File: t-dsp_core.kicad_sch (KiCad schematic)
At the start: 209 parts, among them IC1 Logic Level Shifter - 74HCT2G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, J1 jumper, J10 JST-XH Connector, J11 JST-XH Connector, J12 RGB LED HEADEER, J13 Conn_01x02, J14 Conn_01x03, J15 Conn_01x01, J16 Conn_01x02, J17 Conn_02x04_Odd_Even, J18 Conn_02x02_Odd_Even, J19 Conn_01x01, J2 GROUND HEADER, J20 Conn_01x01, J21 jumper, J22 35RAPC4BV4, J23 35RAPC4BV4, J24 Conn_01x04, J25 PRT-14417, J26 73725-0110BLF, J3 jumper, J4 jumper, J5 jumper, J6 jumper, J7 jumper, J8 PJRAS2X1S01X, J9 PJRAS2X1S01X, Q1 DMG2307L-7, Q2 DMG2307L-7, SW1 SW_SPST, SW2 TL1105WF160Q - 3.15mm actuator, SW3 SW_SPST, SW4 SW_SPST, SW5 RotaryEncoder_Switch_MP, SW6 TL1105WF160Q - 3.15mm actuator, SW7 TL1105WF160Q - 3.15mm actuator, SW8 TL1105WF160Q - 3.15mm actuator, T108 Tab, T109 Tab, T110 Tab, T111 Tab, U1 Teensy 4.1 - DEVKIT, U10 TPD4E02B04DQA, U2 ESP32-DevKitC - DEVKIT, U3 Power Mux & Protect - TPS2116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, U4 Optoisolators - H11L1SM - 6-S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, U5 Dual Buffer - SN74LVC2G125DCTR, U6 Dual Buffer - SN74LVC2G125DCTR, U7 Dual Buffer - SN74LVC2G125DCTR, U8 Dual Buffer - SN74LVC2G125DCTR, U9 Dual Buffer - 74HCT2G17GW,125

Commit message: Migrate project to KiCad 10 and add clock/filter block
Two changes are combined here because KiCad 10 rewrote every file it
opened, making the format churn inseparable from the design work.

Design work:
- Adds ~43 schematic symbols and 31 footprints: U11, U109, CR1 oscillator,
  FL1/FL2 common-mode chokes, FB8 ferrite, C40-C49, C129, R55-R58, R61,
  and associated wiring, junctions and global labels.
- New library parts: BLM15AG601SN1D, BLM18BA121SN1D, CR_SMA_403AE_OSI,
  DLW32SH101XK2L, C_0402 hand-solder, MSOP-12-1EP, Abracon ASDMB
  oscillator, Tab.
- Registers lib_sch in fp-lib-table.

Format migration:
- All .kicad_mod, .kicad_sch, .kicad_pcb and .kicad_pro files rewritten in
  KiCad 10 format. These will no longer open in KiCad 9.

Also ignores .history/ (VS Code local history) and #auto_saved_files#.

Co-Authored-By: Claude Opus 5 <noreply@anthropic.com>
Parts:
- added C129: 0.1uF, project_fp:C_0402_1005Metric, symbol proejct_lib:C_Small
- added C40: 0.1 uF, project_fp:C_0805_2012Metric_Pad1.15x1.40mm_HandSolder, symbol Device:C_Small
- added C41, C42, C44: 10 uF, project_fp:C_0805_2012Metric_Pad1.15x1.40mm_HandSolder, symbol TEENSY_4.0_ESP32_AUDIO-rescue:C_Small-Device
- added C43: 4.7uF, project_fp:C_0805_2012Metric_Pad1.15x1.40mm_HandSolder, symbol TEENSY_4.0_ESP32_AUDIO-rescue:C_Small-Device
- added C45: 1 uF, project_fp:C_0402_1005Metric_Pad0.74x0.62mm_HandSolder, symbol Device:C
- added C46: 100nF, project_fp:C_0402_1005Metric_Pad0.74x0.62mm_HandSolder, symbol Device:C
- added C47, T*C108, T*C110: 10uF, project_fp:C_0805_2012Metric_Pad1.18x1.45mm_HandSolder, symbol proejct_lib:C_Small
- added C48, T*C109: 1uF, project_fp:C_0603_1608Metric_Pad1.08x0.95mm_HandSolder, symbol proejct_lib:C_Small
- added C49: 100nF, project_fp:C_0402_1005Metric_Pad0.74x0.62mm_HandSolder, symbol Device:C_Small
- added CR1: SS14, lib:CR_SMA_403AE_OSI, symbol CR_SMA_403AE_OSI:SS14
- added FB1, FB8: 600Ω@100MHz, project_fp:BLM15AG601SN1D, symbol Device:FerriteBead_Small
- added FL1: BLM18BA121SN1D, lib_sch:BLM18BA121SN1D, symbol BLM18BA121SN1D:BLM18BA121SN1D
- added FL2: DLW32SH101XK2L, lib:DLW32SH101XK2L, symbol DLW32SH101XK2L:DLW32SH101XK2L
- added G119, J3V108: jumper, project_fp:jumper_slice, symbol proejct_lib:NetTie_2
- added NT108: NetTie_2, project_fp:jumper_slice, symbol proejct_lib:NetTie_2
- added R55, R56: 49.9 ohm, project_fp:R_0805_2012Metric_Pad1.15x1.40mm_HandSolder, symbol Device:R
- added R57: 33.0 k, project_fp:R_0805_2012Metric_Pad1.15x1.40mm_HandSolder, symbol Device:R
- added R58: 300 ohm, project_fp:R_0805_2012Metric_Pad1.15x1.40mm_HandSolder, symbol Device:R
- added R59, R60: 0 ohm, Capacitor_SMD:C_0402_1005Metric_Pad0.74x0.62mm_HandSolder, symbol Device:R
- added R61: 33 ohm, project_fp:R_0805_2012Metric_Pad1.15x1.40mm_HandSolder, symbol Device:R
- added U109: 3.3v LDO - LP5907-3.3, project_fp:SOT-23-5, symbol proejct_lib:TLV70012_SOT23-5
- added U11: Dual Buffer - SN74LVC2G125DCTR, project_fp:SOP65P400X130-8N, symbol SN74LVC2G125DCTR:SN74LVC2G125DCTR
- added U13: LT3045EMSE#TRPBF, Package_SO:MSOP-12-1EP_3x4.039mm_P0.65mm_EP1.651x2.845mm, symbol Regulator_Linear:LT3045xMSE
- added Y1: audio clock, Oscillator:Oscillator_SMD_Abracon_ASDMB-4Pin_2.5x2.0mm, symbol Oscillator:ASDMB-xxxMHz
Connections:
- net 3.3V: now also C129.1, C40.1, FB1.1, J3V108.1, U109.3 (EN), U11.8 (VCC)
- net 5V: now also C47.1, C48.1, C49.1, FB8.2, FL1.1, NT108.1
- net 8_IN1: now also U11.2 (1A); no longer U1.10 (8_TX2_IN1)
- net 9_OUT1C_INPUT: now also U11.5 (2A); no longer U1.11 (9_OUT1C)
- net GND: now also C40.2, C41.2, C42.2, C43.2, C44.2, C45.2, C46.2, C47.2, C48.2, C49.2, FL2.3, R57.1, R58.1, R60.2, U11.1 (~{1OE}), U11.4 (GND), U11.7 (~{2OE}), Y1.2 (GND)
- net MCLK1: now also R61.2
- new net: C44.1, C45.1, C46.1, FB1.2, R59.1, Y1.4 (VDD)
- new net: R59.2, R60.1, Y1.1 (Standby)
- new net: G119.1, T*C108.2, T*C109.2, T*C110.2, U109.2 (GND)
- new net: CR1.1, FB8.1
- new net: CR1.2, FL2.2
- new net: R61.1, Y1.3 (Out)
- new net: C41.1, FL1.2, U13.1 (IN), U13.2 (IN), U13.3 (IN), U13.4 (EN/UV)
- new net: R56.1, U11.3 (2Y)
- new net: R55.1, U11.6 (1Y)
- new net: C42.1, U13.10 (OUTS), U13.11 (OUT), U13.12 (OUT)
- new net: U13.13 (GND), U13.9 (GND)
- new net: R58.2, U13.6 (ILIM)
- new net: C43.1, R57.2, U13.8 (SET)
- new net 3.3V_A: J3V108.2, T*C110.1, U109.5 (OUT)
- new net 5V_THIN: NT108.2, T*C108.1, T*C109.1, U109.1 (IN)
- new net 5V_unfiltered: FL2.1
- new net 8_IN1+: R55.2, U1.10 (8_TX2_IN1)
- new net 9_OUT1C_INPUT+: R56.2, U1.11 (9_OUT1C)
- new net Earth: G119.2
- new net GNDD: C129.2
- new net GND_unfiltered: FL2.4
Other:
- note added: "3.3v DIGITAL RAIL"
- note added: "Low-Jitter Audio Clock"
- note added: "POWER SUPPLY"
- note added: "USB POWER FILTER"
- moved on the sheet: BAT1, BAT2, C1, C10, C11, C12, C13, C14, C15, C16, C17, C18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

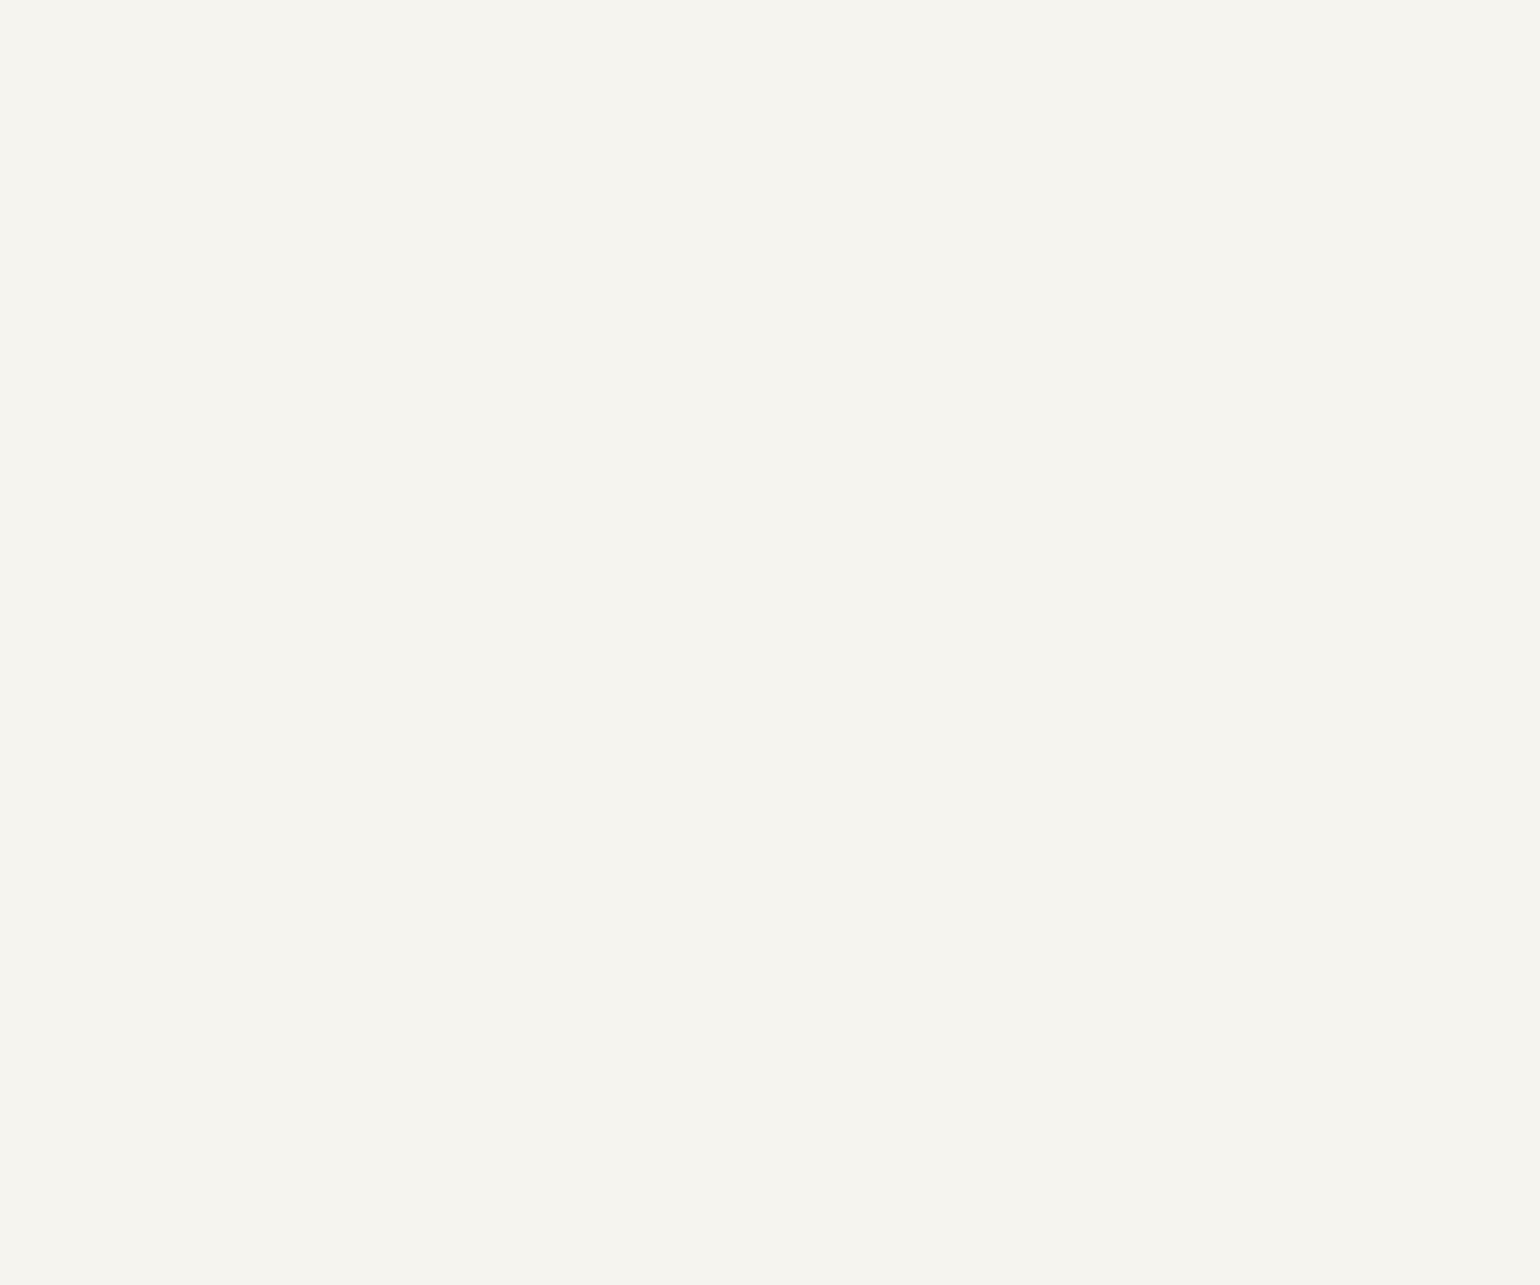
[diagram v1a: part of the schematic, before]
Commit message: Merge ESP32-S3 section from t-dsp-core fork
Brings the ESP32-S3 migration work into this repository, which has the
git history, the origin remote, and the newer clock/filter block. The
t-dsp-core working tree it came from is now redundant.

Pasted section (241 elements at negative X): 106 wires, 64 global labels,
28 symbols, 24 junctions, 11 labels, 7 no-connects, 1 text. Contains a
duplicate of the ESP32 support circuitry with U110 (ESP32-S3-WROOM-1)
placed at its centre, currently unwired.

Seven reference designators collided with the existing clock/filter block
and were reassigned on the pasted copies only, leaving the originals
untouched:

  C43 -> C130    R55 -> R66    R57 -> R68    U13 -> U110
  C44 -> C131    R56 -> R67    R61 -> R69

The section shares all its net labels with the original ESP32-DevKitC
circuit. That resolves when the classic section is excluded from board.

Co-Authored-By: Claude Opus 5 <noreply@anthropic.com>
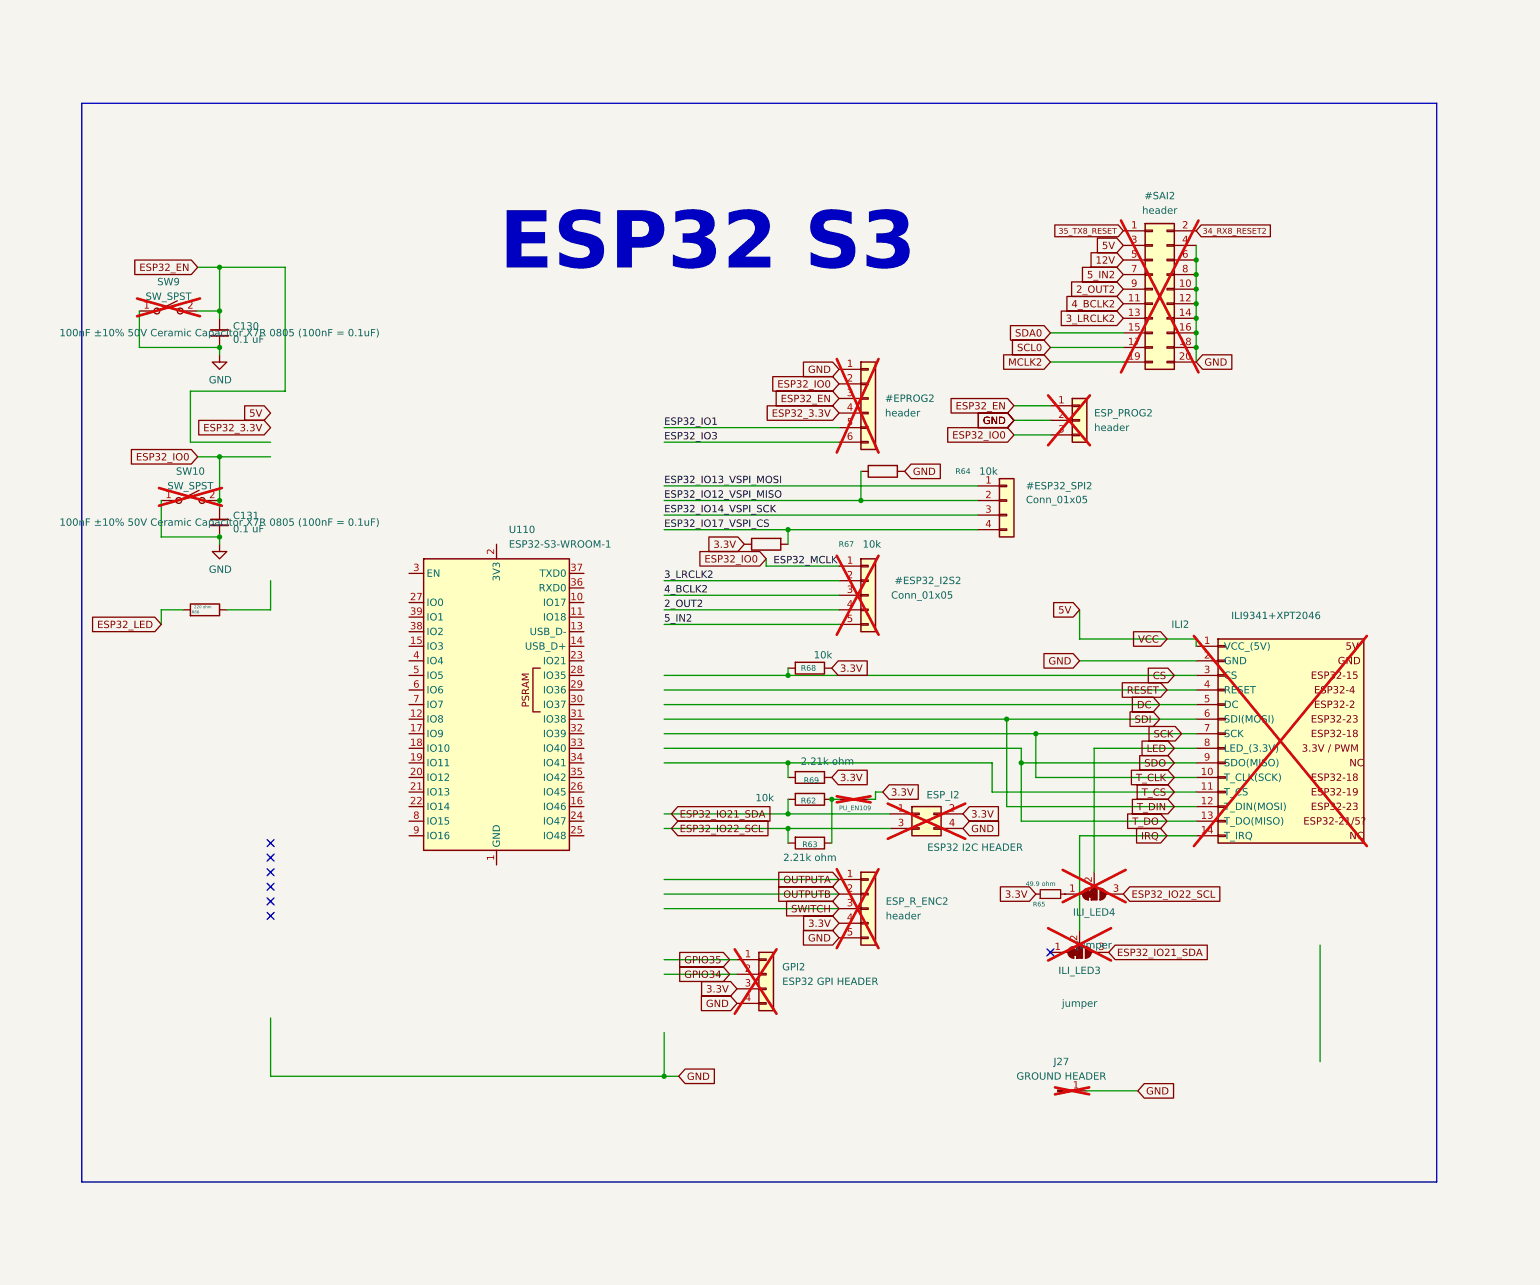
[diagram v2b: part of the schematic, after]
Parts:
- added #EPROG2: header, project_fp:EPROG1_PinHeader_1x06_P2.54mm_Vertical, symbol Connector_Generic:Conn_01x06
- added #ESP32_I2S2: Conn_01x05, Connector_PinHeader_2.54mm:PinHeader_1x05_P2.54mm_Vertical, symbol Connector_Generic:Conn_01x05
- added #ESP32_SPI2: Conn_01x05, Connector_PinHeader_2.54mm:PinHeader_1x05_P2.54mm_Vertical, symbol Connector_Generic:Conn_01x04
- added #SAI2: header, project_fp:IDC-Header_2x10_P2.54mm_Vertical_I2S_expansion, symbol Connector_Generic:Conn_02x10_Odd_Even
- added C130, C131: 0.1 uF, project_fp:C_0805_2012Metric_Pad1.15x1.40mm_HandSolder, symbol TEENSY_4.0_ESP32_AUDIO-rescue:C_Small-Device
- added ESP_I2: ESP32 I2C HEADER, project_fp:ESP_I2C_PinHeader_1x04_P2.54mm_Vertical, symbol Connector_Generic:Conn_02x02_Odd_Even
- added ESP_PROG2: header, project_fp:E_PROG1_PinHeader_1x03_P2.54mm_Vertical, symbol Connector_Generic:Conn_01x03
- added ESP_R_ENC2: header, project_fp:ESP_R_ENC0_PinHeader_1x05_P2.54mm_Vertical, symbol Connector_Generic:Conn_01x05
- added GPI2: ESP32 GPI HEADER, project_fp:GPI1_PinHeader_1x04_P2.54mm_Vertical, symbol Connector_Generic:Conn_01x04
- added ILI2: ILI9341+XPT2046, project_fp:ILI9341_PinHeader_1x14_P2.54mm_Vertical, symbol project_sch:ILI9341_header
- added ILI_LED3, ILI_LED4: jumper, project_fp:SolderJumper-3_P1.3mm_Bridged2Bar12_Pad1.0x1.5mm_NumberLabels, symbol Jumper:SolderJumper_3_Bridged12
- added J27: GROUND HEADER, project_fp:GPIO_GROUND_PinHeader_1x01_P2.54mm_Vertical, symbol Connector:Conn_01x01_Pin
- added PU_EN109: JUMPER, project_fp:SolderJumper-2_Open_Pad0.5x1.0mm_PU, symbol proejct_lib:NetTie_2
- added R62, R63: 2.21k ohm, project_fp:R_0805_2012Metric_Pad1.15x1.40mm_HandSolder, symbol Device:R
- added R64, R67, R68, R69: 10k, project_fp:R_0805_2012Metric_Pad1.15x1.40mm_HandSolder, symbol Device:R
- added R65: 49.9 ohm, project_fp:R_0805_2012Metric_Pad1.15x1.40mm_HandSolder, symbol proejct_lib:R_Small
- added R66: 220 ohm, project_fp:R_0805_2012Metric_Pad1.20x1.40mm_HandSolder, symbol Device:R
- added SW10, SW9: SW_SPST, project_fp:SW_Tactile_SPST_Angled_PTS645Vx39-2LFS, symbol Switch:SW_SPST
- added U110: ESP32-S3-WROOM-1, RF_Module:ESP32-S3-WROOM-1U, symbol RF_Module:ESP32-S3-WROOM-1
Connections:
- net 12V: now also #SAI2.5 (Pin_5)
- net 2_OUT2: now also #ESP32_I2S2.4 (Pin_4), #SAI2.9 (Pin_9)
- net 3.3V: now also ESP_I2.2 (Pin_2), ESP_R_ENC2.4 (Pin_4), GPI2.3 (Pin_3), PU_EN109.1, R65.1, R67.1, R68.1, R69.1
- net 34_RX8_RESET2: now also #SAI2.2 (Pin_2)
- net 35_TX8_RESET: now also #SAI2.1 (Pin_1)
- net 3_LRCLK2: now also #ESP32_I2S2.2 (Pin_2), #SAI2.13 (Pin_13)
- net 4_BCLK2: now also #ESP32_I2S2.3 (Pin_3), #SAI2.11 (Pin_11)
- net 5V: now also #SAI2.3 (Pin_3), ILI2.1 (VCC_(5V))
- net 5_IN2: now also #ESP32_I2S2.5 (Pin_5), #SAI2.7 (Pin_7)
- net CS: now also ILI2.3 (CS), R68.2
- net DC: now also ILI2.5 (DC)
- net ESP32_3.3V: now also #EPROG2.4 (Pin_4)
- net ESP32_EN: now also #EPROG2.3 (Pin_3), C130.1, ESP_PROG2.1 (Pin_1), SW9.2 (B)
- net ESP32_IO0: now also #EPROG2.2 (Pin_2), #ESP32_I2S2.1 (Pin_1), C131.1, ESP_PROG2.3 (Pin_3), SW10.2 (B)
- net ESP32_IO1: now also #EPROG2.5 (Pin_5)
- net ESP32_IO12_SPI_MISO: now also #ESP32_SPI2.2 (Pin_2), R64.1
- net ESP32_IO13_SPI_MOSI: now also #ESP32_SPI2.1 (Pin_1)
- net ESP32_IO14_SPI_SCK: now also #ESP32_SPI2.3 (Pin_3)
- net ESP32_IO21_SDA: now also ESP_I2.1 (Pin_1), ILI_LED3.3 (B), R62.2
- net ESP32_IO22_SCL: now also ESP_I2.3 (Pin_3), ILI_LED4.3 (B), R63.2
- net ESP32_IO3: now also #EPROG2.6 (Pin_6)
- net ESP32_IO33_SPI_CS: now also #ESP32_SPI2.4 (Pin_4), R67.2
- net ESP32_LED: now also R66.2
- net GND: now also #EPROG2.1 (Pin_1), #SAI2.10 (Pin_10), #SAI2.12 (Pin_12), #SAI2.14 (Pin_14), #SAI2.16 (Pin_16), #SAI2.18 (Pin_18), #SAI2.20 (Pin_20), #SAI2.4 (Pin_4), #SAI2.6 (Pin_6), #SAI2.8 (Pin_8), C130.2, C131.2, ESP_I2.4 (Pin_4), ESP_PROG2.2 (Pin_2), ESP_R_ENC2.5 (Pin_5), GPI2.4 (Pin_4), ILI2.2 (GND), J27.1 (Pin_1), R64.2, SW10.1 (A), SW9.1 (A)
- net GPIO34: now also GPI2.2 (Pin_2)
- net GPIO35: now also GPI2.1 (Pin_1)
- net IRQ: now also ILI2.14 (T_IRQ), ILI_LED3.2 (C)
- net LED: now also ILI2.8 (LED_(3.3V)), ILI_LED4.2 (C)
- net MCLK2: now also #SAI2.19 (Pin_19)
- net OUTPUTA: now also ESP_R_ENC2.1 (Pin_1)
- net OUTPUTB: now also ESP_R_ENC2.2 (Pin_2)
- net RESET: now also ILI2.4 (RESET)
- net SCK: now also ILI2.10 (T_CLK(SCK)), ILI2.7 (SCK)
- net SCL0: now also #SAI2.17 (Pin_17)
- net SDA0: now also #SAI2.15 (Pin_15)
- net SDI: now also ILI2.12 (T_DIN(MOSI)), ILI2.6 (SDI(MOSI))
- net SDO: now also ILI2.13 (T_DO(MISO)), ILI2.9 (SDO(MISO))
- net SWITCH: now also ESP_R_ENC2.3 (Pin_3)
- net T_CS: now also ILI2.11 (T_CS), R69.2
- new net: PU_EN109.2, R62.1, R63.1
- new net: U110.1 (GND), U110.40 (GND), U110.41 (GND)
- new net: ILI_LED4.1 (A), R65.2
- no-connect marks 21 -> 28
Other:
- note added: "ESP32 S3"

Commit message: Wire U110 (ESP32-S3) to the migrated net map
Connects 19 of 41 pins on U110, replacing the ESP32-DevKitC pinout with
ESP32-S3-WROOM-1 equivalents. Each connection is a 5.08mm wire stub plus a
label matching the type already used for that net elsewhere on the sheet.

Carried over unchanged:
  3V3->2  EN->3  GND->1/40/41  IO0->27  IO12->20  IO13->21  IO14->22
  IO16->9  IO17->10  IO39->32 (OUTPUTB)

Reassigned - no equivalent pin exists on the S3:
  2_OUT2   GPIO33 -> IO4   (pin 4)
  4_BCLK2  GPIO26 -> IO6   (pin 6)
  5_IN2    GPIO25 -> IO7   (pin 7)
  SWITCH   GPIO27 -> IO15  (pin 8)

Moved deliberately:
  OUTPUTA  GPIO36 -> IO38  (pin 31) - IO35-37 are consumed by octal PSRAM
  ESP32_IO1  U0TXD -> TXD0 (pin 37) - UART0 relocated on the S3
  ESP32_IO3  U0RXD -> RXD0 (pin 36)

Still outstanding: the 5V net has no home on a bare module (the DevKitC
supplied its own LDO), and USB_D-/D+ (pins 13/14) are unconnected pending
the native-USB front end. Both belong to the support-circuitry pass.

Co-Authored-By: Claude Opus 5 <noreply@anthropic.com>
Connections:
- net 2_OUT2: now also U110.4 (IO4)
- net 3_LRCLK2: now also U110.9 (IO16)
- net 4_BCLK2: now also U110.6 (IO6)
- net 5_IN2: now also U110.7 (IO7)
- net ESP32_3.3V: now also U110.2 (3V3)
- net ESP32_EN: now also U110.3 (EN)
- net ESP32_IO0: now also U110.27 (IO0)
- net ESP32_IO1: now also U110.37 (TXD0)
- net ESP32_IO12_SPI_MISO: now also U110.20 (IO12)
- net ESP32_IO13_SPI_MOSI: now also U110.21 (IO13)
- net ESP32_IO14_SPI_SCK: now also U110.22 (IO14)
- net ESP32_IO3: now also U110.36 (RXD0)
- net ESP32_IO33_SPI_CS: now also U110.10 (IO17)
- net GND: now also U110.1 (GND), U110.40 (GND), U110.41 (GND)
- net OUTPUTA: now also U110.31 (IO38)
- net OUTPUTB: now also U110.32 (IO39)
- net SWITCH: now also U110.8 (IO15)
